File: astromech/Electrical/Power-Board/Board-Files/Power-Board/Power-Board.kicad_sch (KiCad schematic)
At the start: 42 parts, among them Q1 Q_NMOS_DSG, Q2 Q_NMOS_DSG, U1 LTC7003, U2 LTC7003

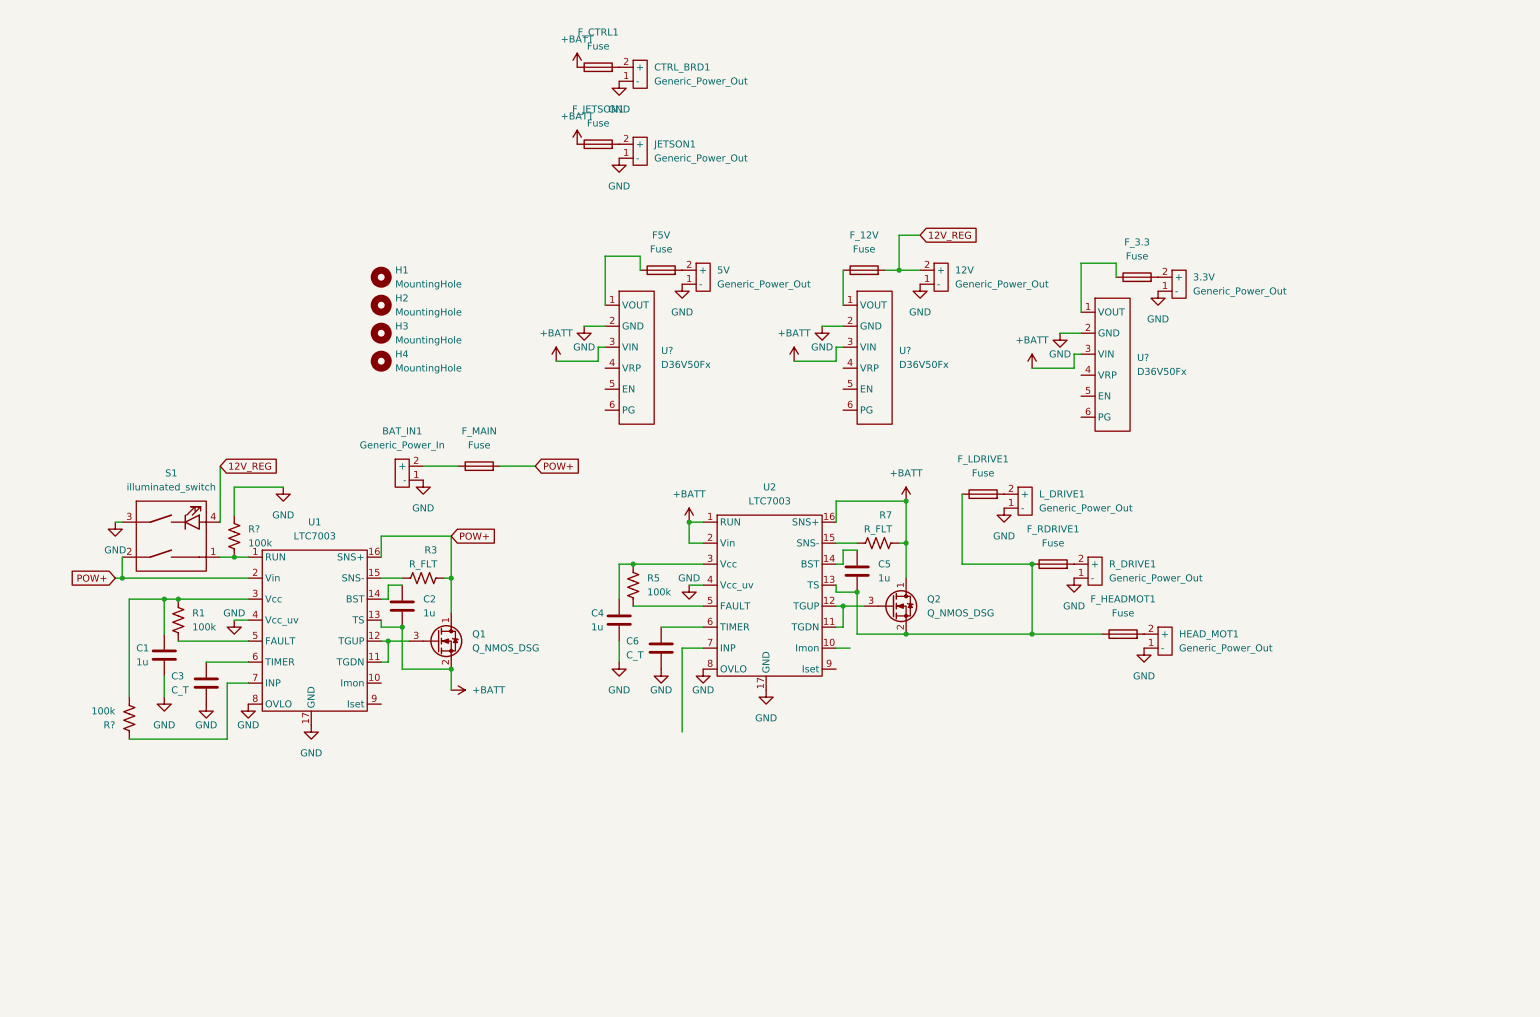
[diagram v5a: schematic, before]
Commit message: updated checklist and neatened schematic
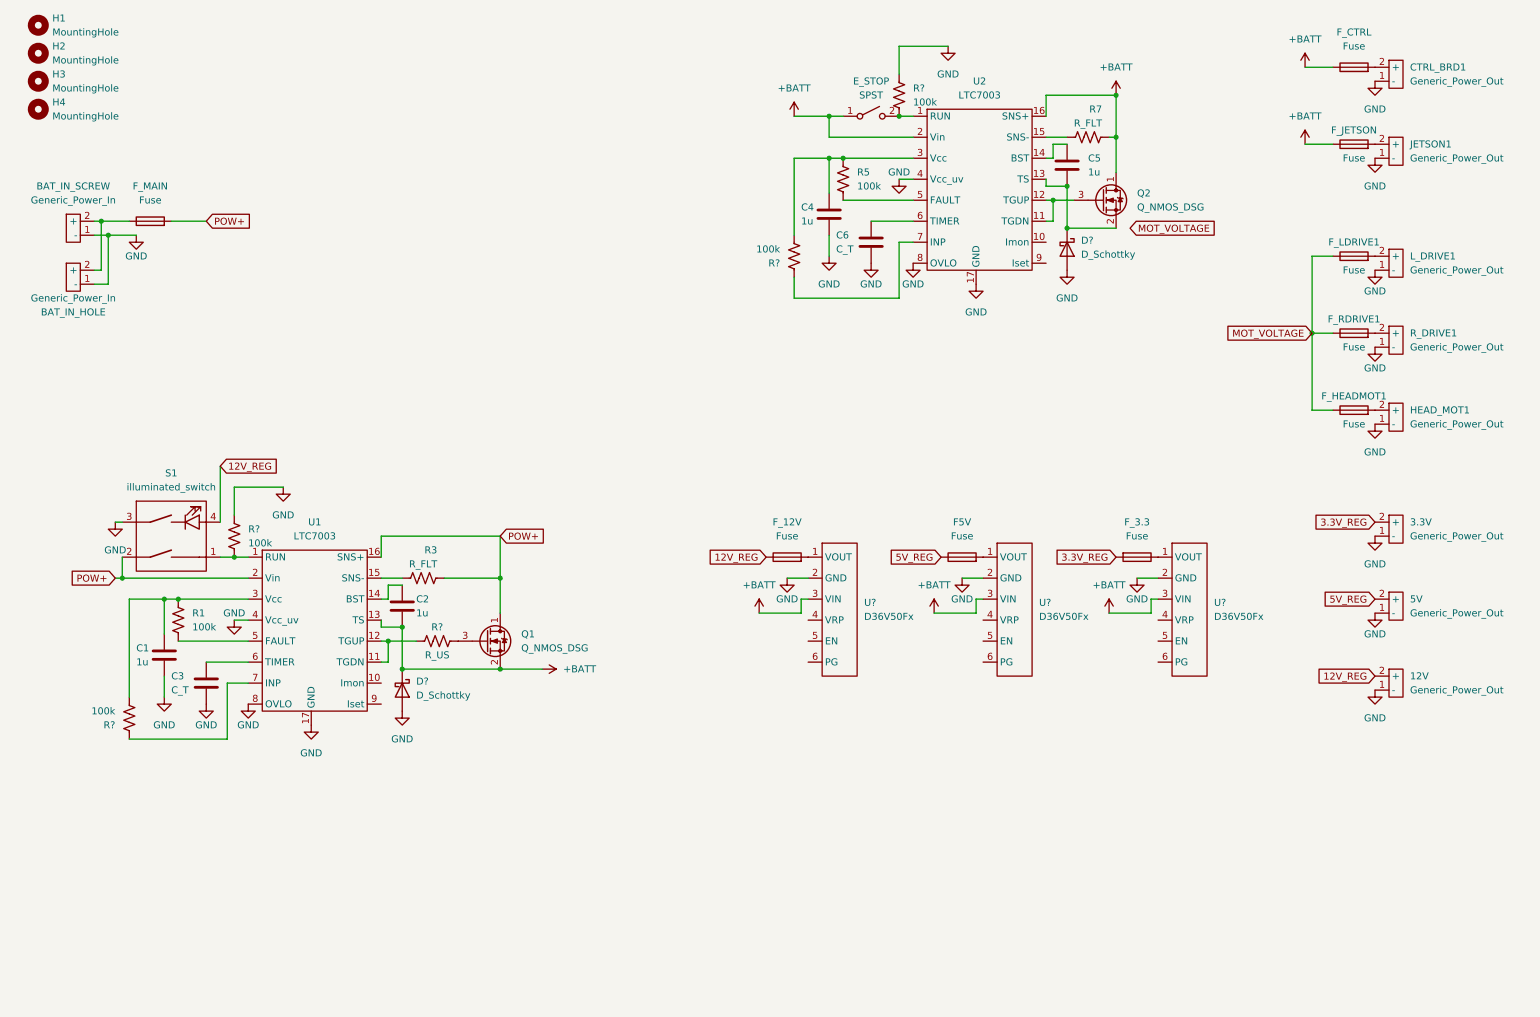
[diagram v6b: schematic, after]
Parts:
- added BAT_IN_HOLE: Generic_Power_In, symbol astromech-power-board:Generic_Power_In
- added D? (x2): D_Schottky, symbol Device:D_Schottky
- added E_STOP: SPST, symbol Switch:SW_SPST
- added R?: R_US, symbol Device:R_US
- added R? (x2): 100k, symbol Device:R_US
- renumbered BAT_IN1 to BAT_IN_SCREW, F_CTRL1 to F_CTRL, F_JETSON1 to F_JETSON
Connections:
- net +BATT: now also D?.1 (K), E_STOP.1 (A); no longer U2.1 (RUN)
- net 12V_REG: now also F_12V.1; no longer F_12V.2
- net GND: now also BAT_IN_HOLE.1 (-), D?.2 (A), D?.2 (A), R?.1
- net at C5.2, Q2.2 (S), U2.13 (TS): now also D?.1 (K); no longer F_HEADMOT1.1, F_LDRIVE1.1, F_RDRIVE1.1
- net at U?.1 (VOUT): now also F5V.2; no longer F5V.1
- net at C4.1, R5.1, U2.3 (Vcc): now also R?.2
- net at U2.7 (INP): now also R?.1
- net 3.3V_REG: now reaches 3.3V.2 (+), F_3.3.2
- net at BAT_IN_SCREW.2 (+), F_MAIN.1: now also BAT_IN_HOLE.2 (+)
- net at U1.11 (TGDN), U1.12 (TGUP): now also R?.1; no longer Q1.3 (G)
- net at U?.1 (VOUT): now also F_12V.2; no longer F_12V.1
- net 5V_REG: now reaches 5V.2 (+)
- net 5V_REG: now also F5V.1; no longer F5V.2
- new net: Q1.3 (G), R?.2
- new net: E_STOP.2 (B), R?.2, U2.1 (RUN)
- new net MOT_VOLTAGE: F_HEADMOT1.1, F_LDRIVE1.1, F_RDRIVE1.1
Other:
- moved on the sheet: 12V, 3.3V, 5V, BAT_IN_SCREW, C4, C5, C6, CTRL_BRD1, F5V, F_12V, F_3.3, F_CTRL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

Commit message: Added mosfet footprint
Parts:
- Q1, Q2: footprint (none) -> astromech-footprints:NTMTS0D6N04CLTXG
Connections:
- net MOT_VOLTAGE: now also C5.2, D?.1 (K), Q2.2 (S), U2.13 (TS)
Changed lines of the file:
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@@
   (junction (at 203.2 45.72) (diameter 0) (color 0 0 0 0)
   )
+  (junction (at 212.09 53.34) (diameter 0) (color 0 0 0 0)
+  )
   (junction (at 203.2 53.34) (diameter 0) (color 0 0 0 0)
   )
@@
     (stroke (width 0) (type default) (color 0 0 0 0))
   )
+  (wire (pts (xy 215.9 53.34) (xy 212.09 53.34))
+    (stroke (width 0) (type default) (color 0 0 0 0))
+  )
   (wire (pts (xy 80.01 128.27) (xy 80.01 132.08))
     (stroke (width 0) (type default) (color 0 0 0 0))
@@
     (stroke (width 0) (type default) (color 0 0 0 0))
   )
+  (wire (pts (xy 212.09 53.34) (xy 203.2 53.34))
+    (stroke (width 0) (type default) (color 0 0 0 0))
+  )
   (wire (pts (xy 210.82 36.83) (xy 212.09 36.83))
     (stroke (width 0) (type default) (color 0 0 0 0))
@@
   )
   (wire (pts (xy 46.99 52.07) (xy 40.64 52.07))
-    (stroke (width 0) (type default) (color 0 0 0 0))
-  )
-  (wire (pts (xy 212.09 53.34) (xy 203.2 53.34))
     (stroke (width 0) (type default) (color 0 0 0 0))
   )
@@
     )
   )
-  (global_label "MOT_VOLTAGE" (shape input) (at 214.63 53.34 0) (fields_autoplaced)
+  (global_label "MOT_VOLTAGE" (shape input) (at 215.9 53.34 0) (fields_autoplaced)
     (effects (font (size 1.27 1.27)) (justify left))
-    (property "Intersheet References" "${INTERSHEET_REFS}" (id 0) (at 229.6826 53.2606 0)
+    (property "Intersheet References" "${INTERSHEET_REFS}" (id 0) (at 230.9526 53.2606 0)
       (effects (font (size 1.27 1.27)) (justify left) hide)
     )
@@
       (effects (font (size 1.27 1.27)) (justify left))
     )
-    (property "Footprint" "" (id 2) (at 102.87 125.73 0)
+    (property "Footprint" "astromech-footprints:NTMTS0D6N04CLTXG" (id 2) (at 102.87 125.73 0)
       (effects (font (size 1.27 1.27)) hide)
     )
@@
       (effects (font (size 1.27 1.27)) (justify left))
     )
-    (property "Footprint" "" (id 2) (at 214.63 45.72 0)
+    (property "Footprint" "astromech-footprints:NTMTS0D6N04CLTXG" (id 2) (at 214.63 45.72 0)
       (effects (font (size 1.27 1.27)) hide)
     )
@@
     )
     (path "/8d35852c-b961-4ac3-b078-a501ab041ffc"
-      (reference "Q1") (unit 1) (value "Q_NMOS_DSG") (footprint "")
+      (reference "Q1") (unit 1) (value "Q_NMOS_DSG") (footprint "astromech-footprints:NTMTS0D6N04CLTXG")
     )
     (path "/9706bcfd-5f44-4b66-8572-92b7d2601c22"
-      (reference "Q2") (unit 1) (value "Q_NMOS_DSG") (footprint "")
+      (reference "Q2") (unit 1) (value "Q_NMOS_DSG") (footprint "astromech-footprints:NTMTS0D6N04CLTXG")
     )
     (path "/18f12ad4-289b-4a2d-90b3-4918f001cb40"

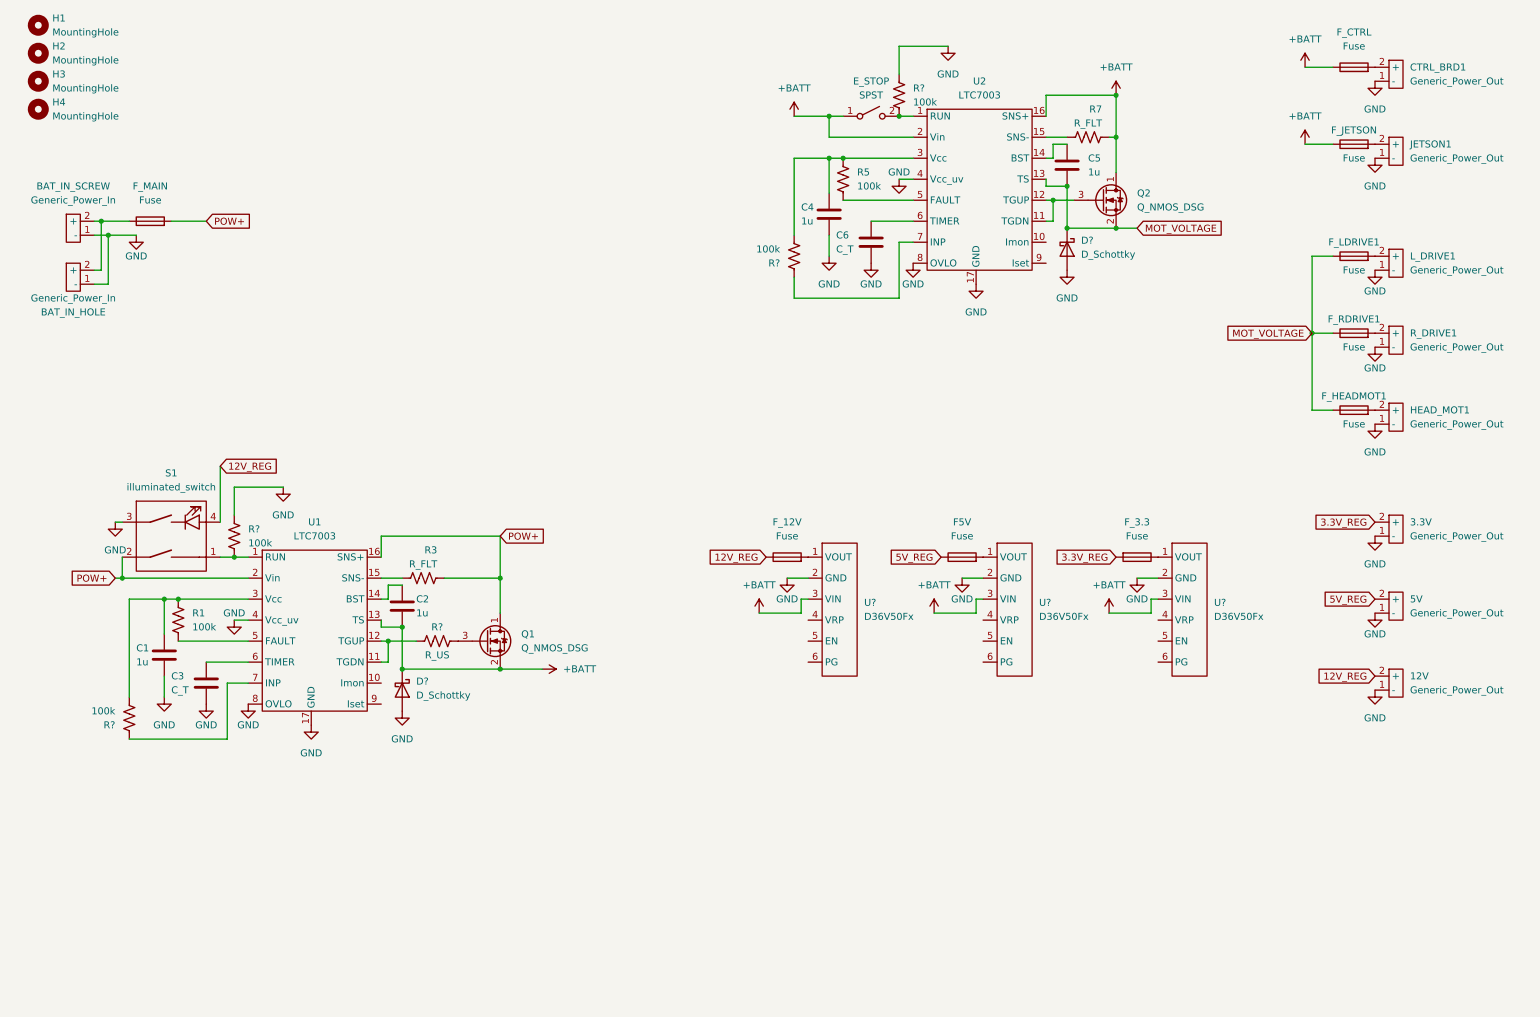
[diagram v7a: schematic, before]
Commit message: finished LTC7003 implementation
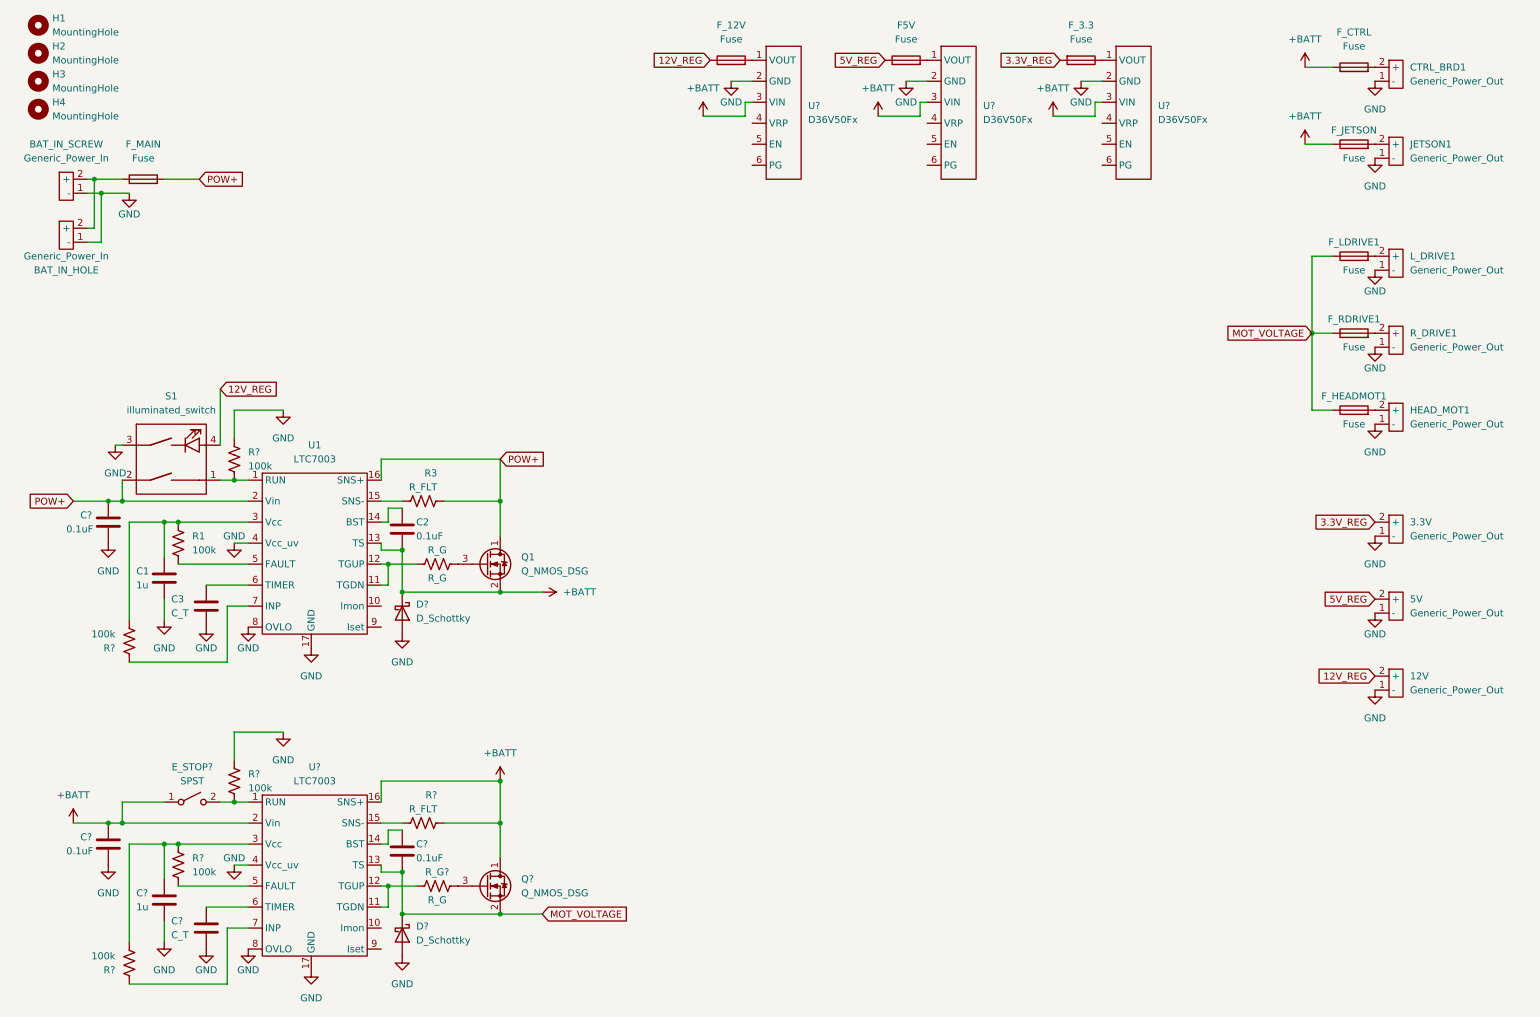
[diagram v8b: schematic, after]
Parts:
- removed C4, C5: 1u, symbol Device:C
- removed C6: C_T, symbol Device:C
- removed D?: D_Schottky, symbol Device:D_Schottky
- removed E_STOP: SPST, symbol Switch:SW_SPST
- removed Q2: Q_NMOS_DSG, astromech-footprints:NTMTS0D6N04CLTXG, symbol Device:Q_NMOS_DSG
- removed R5, R? (x2): 100k, symbol Device:R_US
- removed R7: R_FLT, symbol Device:R_US
- removed U2: LTC7003, astromech-footprints:LTC7003, symbol astromech-power-board:LTC7003
- added C? (x3): 0.1uF, symbol Device:C
- added C?: 1u, symbol Device:C
- added C?: C_T, symbol Device:C
- added D?: D_Schottky, symbol Device:D_Schottky
- added E_STOP?: SPST, symbol Switch:SW_SPST
- added Q?: Q_NMOS_DSG, astromech-footprints:NTMTS0D6N04CLTXG, symbol Device:Q_NMOS_DSG
- added R? (x3): 100k, symbol Device:R_US
- added R?: R_FLT, symbol Device:R_US
- added R_G?: R_G, symbol Device:R_US
- added U?: LTC7003, astromech-footprints:LTC7003, symbol astromech-power-board:LTC7003
- C2: value 1u -> 0.1uF
- R_G: renamed from R?; value R_US -> R_G
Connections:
- net +BATT: now also C?.1, E_STOP?.1 (A), Q?.1 (D), R?.2, U?.16 (SNS+), U?.2 (Vin)
- net GND: now also C?.2, C?.2, C?.2, C?.2, D?.2 (A), R?.1, U?.17 (GND), U?.4 (Vcc_uv), U?.8 (OVLO)
- net MOT_VOLTAGE: now also C?.2, D?.1 (K), Q?.2 (S), U?.13 (TS)
- net POW+: now also C?.1
- new net: E_STOP?.2 (B), R?.2, U?.1 (RUN)
- new net: R_G?.1, U?.11 (TGDN), U?.12 (TGUP)
- new net: C?.1, U?.14 (BST)
- new net: R?.1, U?.15 (SNS-)
- new net: C?.1, R?.1, R?.2, U?.3 (Vcc)
- new net: R?.2, U?.5 (FAULT)
- new net: C?.1, U?.6 (TIMER)
- new net: R?.1, U?.7 (INP)
- new net: Q?.3 (G), R_G?.2
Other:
- moved on the sheet: BAT_IN_HOLE, BAT_IN_SCREW, C1, C2, C3, D?, F5V, F_12V, F_3.3, F_MAIN, Q1, R1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
